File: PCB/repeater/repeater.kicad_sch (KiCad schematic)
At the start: 34 parts, among them J2 RF_IN, U1 DRA818V, U2 DRA818U, U3 PGA-103

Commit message: Continue routing
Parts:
- added C16: 6.8pF, symbol Device:C
- added C17: 12pF, symbol Device:C
- added C18: 10pF, symbol Device:C
- added C19, C20, C21, C22, C23: 100nF, symbol Device:C
- added C24: 10uF, symbol Device:C
- added J1: TX, symbol Connector:Conn_Coaxial
- added L7: 27nH, symbol Device:L
- added L8: 30nH, symbol Device:L
- added L9: 18nH, symbol Device:L
- added R4: 10k, symbol Device:R
- added R5: 10k, Resistor_SMD:R_0603_1608Metric_Pad0.98x0.95mm_HandSolder, symbol Device:R
- added RV1: 10k, symbol Device:R_Potentiometer
- added SW1: SW_Push, symbol Switch:SW_Push
- added U4: STM32F103C8Tx, Package_QFP:LQFP-48_7x7mm_P0.5mm, symbol MCU_ST_STM32F1:STM32F103C8Tx
- J2: value RF_IN -> RX
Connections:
- net AF_OUT: now also C15.1
- net GND: now also C16.2, C17.2, C18.2, C19.1, C20.1, C21.1, C22.1, C23.1, J1.2 (Ext), R5.2, RV1.3, SW1.1, U4.23 (VSS), U4.35 (VSS), U4.47 (VSS), U4.8 (VSSA)
- net VCC_3.3: now also C19.2, C20.2, C21.2, C22.2, C23.2, R4.1, U4.1 (VBAT), U4.24 (VDD), U4.36 (VDD), U4.48 (VDD), U4.9 (VDDA)
- net LPF_IN: now reaches U2.12 (ANT)
- net LPF_IN: now also C16.1, L7.1
- net at U2.18 (MIC_IN): now also RV1.1; no longer C15.2
- new net: C24.1, R4.2, SW1.2, U4.7 (NRST)
- new net: C15.2, RV1.2
- new net: R5.1, U4.44 (BOOT0)
- new net: C18.1, L8.2, L9.1
- new net: C17.1, L7.2, L8.1
- new net: J1.1 (In), L9.2
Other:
- note added: "Receiver BPF (~130MHz to ~150MHz)"
- note added: "Transmitter LPF"
- note added: "UHF Transmitter"
- note added: "Volume adjustment"
- note removed: "Receiver BPF"
- moved on the sheet: C15, D3, JP1, R2, R3, U2

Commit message: more work
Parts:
- added C25, C26: 15pF, symbol Device:C
- added C27, C28: 14pF, symbol Device:C
- added C29, C37, C38, C39, C40: 10uF, Capacitor_SMD:C_0603_1608Metric_Pad1.08x0.95mm_HandSolder, symbol Device:C
- added C30: 220nF, Capacitor_SMD:C_0603_1608Metric_Pad1.08x0.95mm_HandSolder, symbol Device:C
- added C31: 1uF, Capacitor_SMD:C_0603_1608Metric_Pad1.08x0.95mm_HandSolder, symbol Device:C
- added C32: 0.1uF, Capacitor_SMD:C_0603_1608Metric_Pad1.08x0.95mm_HandSolder, symbol Device:C
- added C33, C34, C35, C36: 22uF, Capacitor_SMD:C_0603_1608Metric_Pad1.08x0.95mm_HandSolder, symbol Device:C
- added C41, C42, C43, C44, C45, C46: 100nF, symbol Device:C
- added C47: 510nF, symbol Device:C
- added C48: 68nF, symbol Device:C
- added D4, D5, D6: LED, symbol Device:LED
- added FB1, FB2: FerriteBead, symbol Device:FerriteBead
- added J3: Conn_02x03_Counter_Clockwise, symbol Connector_Generic:Conn_02x03_Counter_Clockwise
- added L10: 8uH, lcsc:IND_BOURNS_SRP1250, symbol Device:L
- added L11: 33mH, symbol Device:L
- added L12: 240mH, symbol Device:L
- added R10: 24.9k, Resistor_SMD:R_0603_1608Metric_Pad0.98x0.95mm_HandSolder, symbol Device:R
- added R6, R7, R8: 1k, symbol Device:R
- added R9 (x2): 100k, Resistor_SMD:R_0603_1608Metric_Pad0.98x0.95mm_HandSolder, symbol Device:R
- added RV2: 10k, symbol Device:R_Potentiometer
- added SW2, SW3: SW_SPDT, symbol Switch:SW_SPDT
- added TP3 (x2): TestPoint, Connector_Pin:Pin_D1.1mm_L8.5mm_W2.5mm_FlatFork, symbol Connector:TestPoint
- added U5: LMR33630ADDA, Package_SO:Texas_HSOP-8-1EP_3.9x4.9mm_P1.27mm_ThermalVias, symbol Regulator_Switching:LMR33630ADDA
- added U6: AMS1117-3.3, Package_TO_SOT_SMD:SOT-223-3_TabPin2, symbol Regulator_Linear:AMS1117-3.3
- added U7: AMS1117-5.0, Package_TO_SOT_SMD:SOT-223-3_TabPin2, symbol Regulator_Linear:AMS1117-3.3
- added Y1: 32.768KHz 12.5pF, symbol Device:Crystal
- added Y2: 8MHz 12pF, symbol Device:Crystal_GND24
- C10, C9: value C -> 10pF
- C11: value 10pF -> 1000pF
- C2, C5: value C -> 3.3pF
- C3, C4: value C -> 9.1pF
- C6, C8: value C -> 2.7pF
- C7: value C -> 2.2pF
- L2, L3, L4, L5: value L -> 100nH
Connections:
- net BPF_IN: now also J2.1 (In)
- net BPF_OUT: now also C1.1, D1.3 (K), TP1.1
- net GND: now also C25.1, C26.1, C27.1, C28.1, C29.2, C30.2, C31.2, C33.2, C34.2, C35.2, C36.2, C37.2, C38.2, C39.2, C40.2, C41.1, C42.1, C43.1, C44.1, C45.1, C46.1, C48.1, D4.1 (K), D5.1 (K), D6.1 (K), J3.5 (Pin_5), L12.1, R10.2, RV2.3, U5.1 (GND), U5.9 (GND), U6.1 (GND), U7.1 (GND), Y2.2, Y2.4
- net PTT: now also U4.42 (PB6)
- net RXD_RX: now also U4.30 (PA9)
- net RXD_TX: now also U4.12 (PA2)
- net SQ: now also U4.43 (PB7)
- net TXD_RX: now also U4.31 (PA10)
- net TXD_TX: now also U4.13 (PA3)
- net VCC: now also C37.1, C40.1, C41.2, C42.2, C43.2, C44.2, C45.2, C46.2, FB1.2, SW3.1 (A), U6.3 (VI), U7.2 (VO)
- net VCC_3.3: now also FB2.2, J3.4 (Pin_4), R6.2, SW3.3 (C); no longer C12.2, C13.2, C14.2, L6.1
- net RST: now reaches C24.1, R4.2, SW1.2, U4.7 (NRST)
- net RST: now also J3.3 (Pin_3)
- net at RV1.1, U2.18 (MIC_IN): now also RV2.1
- net MORSE: now reaches U4.10 (PA0)
- net MORSE: now also RV2.2
- net RCC_OSC32_IN: now reaches U4.3 (PC14)
- net RCC_OSC32_IN: now also C26.2, Y1.1
- net SYS_JTMS-SWDIO: now reaches U4.34 (PA13)
- net SYS_JTMS-SWDIO: now also J3.1 (Pin_1)
- net SYS_JTCK-SWCLK: now reaches U4.37 (PA14)
- net SYS_JTCK-SWCLK: now also J3.2 (Pin_2)
- net RCC_OSC32_OUT: now reaches U4.4 (PC15)
- net RCC_OSC32_OUT: now also C25.2, Y1.2
- net LED_TX: now reaches U4.45 (PB8)
- net LED_TX: now also R7.2
- net LED_RX: now reaches U4.46 (PB9)
- net LED_RX: now also R8.2
- net X_IN: now reaches U4.5 (PD0)
- net X_IN: now also C28.2, Y2.3
- net X_OUT: now reaches U4.6 (PD1)
- net X_OUT: now also C27.2, Y2.1
- new net: D5.2 (A), R7.1
- new net: C12.2, C13.2, C14.2, L6.1, SW3.2 (B)
- new net: C33.1, C34.1, C35.1, C36.1, FB1.1, L10.2, R9.1, TP3.1
- new net: R10.1, R9.2, U5.5 (FB)
- new net: C38.1, FB2.1, U6.2 (VO)
- new net: D4.2 (A), R6.1
- new net: C29.1, C30.1, SW2.1 (A), U5.2 (VIN), U5.3 (EN)
- new net: C31.1, R9.2, U5.6 (VCC)
- new net: C32.1, U5.7 (BOOT)
- new net: C32.2, L10.1, U5.8 (SW)
- new net: C39.1, SW2.3 (C), U7.3 (VI)
- new net: D6.2 (A), R8.1
- new net: C47.2, L11.1
- new net AUDIO_FILTER_IN: C47.1
- new net AUDIO_FILTER_OUT: C48.2, L11.2, L12.2
- new net PG: R9.1, TP3.1, U5.4 (PG)
- new net VCC_IN: J3.6 (Pin_6), SW2.2 (B)
- no-connect marks 4 -> 26
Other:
- note added: "Audio Conditioning Filter (~300Hz to 5KHz)"
- note added: "MCU"
- note added: "No, this is not a mistake - it's either floating or LOW for some reason"
- note added: "Oh boy do I love the 'ol AVR ISP headers"
- note added: "Power supply"
- note added: "Protection diodes...."
- note added: "Theoretical response @200 ohm input 680 ohms output, which is my best guess at the audio impedance"
- note added: "This switch decides how much power we feed into the LNA. More voltage = better gain but also more noise."
- note added: "This switch decides how we generate the 5V rail - SMPS or LDO?"
- note added: "Transmitter LPF ~(465MHz)"
- note added: "Volume adjustment of morse identification"
- note added: "Volume adjustment of repeater"
- note removed: "Transmitter LPF"
- note removed: "Volume adjustment"
- moved on the sheet: C10, C19, C2, C20, C21, C22, C23, C24, C3, C4, C5, C6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

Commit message: Add filter and switch
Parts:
- added SW4: SW_SPDT, symbol Switch:SW_SPDT
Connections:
- net AUDIO_FILTER_IN: now also C15.2, SW4.3 (C)
- net AUDIO_FILTER_OUT: now also SW4.1 (A)
- net at RV1.2: now also SW4.2 (B); no longer C15.2
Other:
- note added: "Switch to turn audio filter on/off"
- moved on the sheet: C15, C44, C45, C46, D2, R1, U1

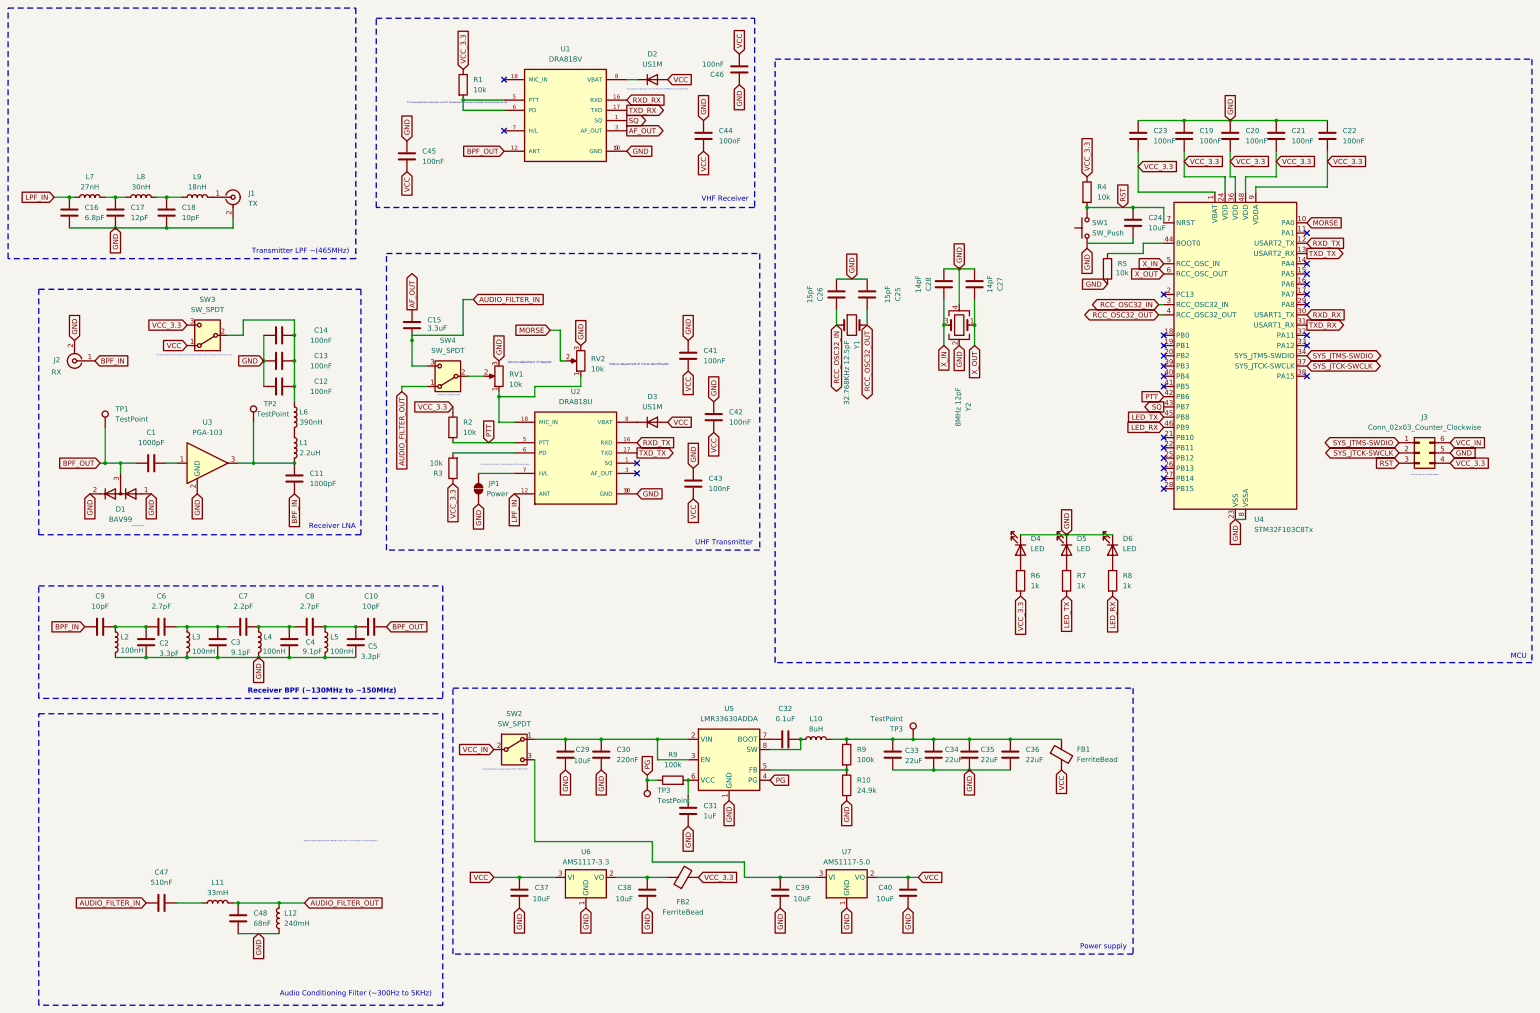
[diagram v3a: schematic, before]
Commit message: Add PD reset pins for all DRA818s
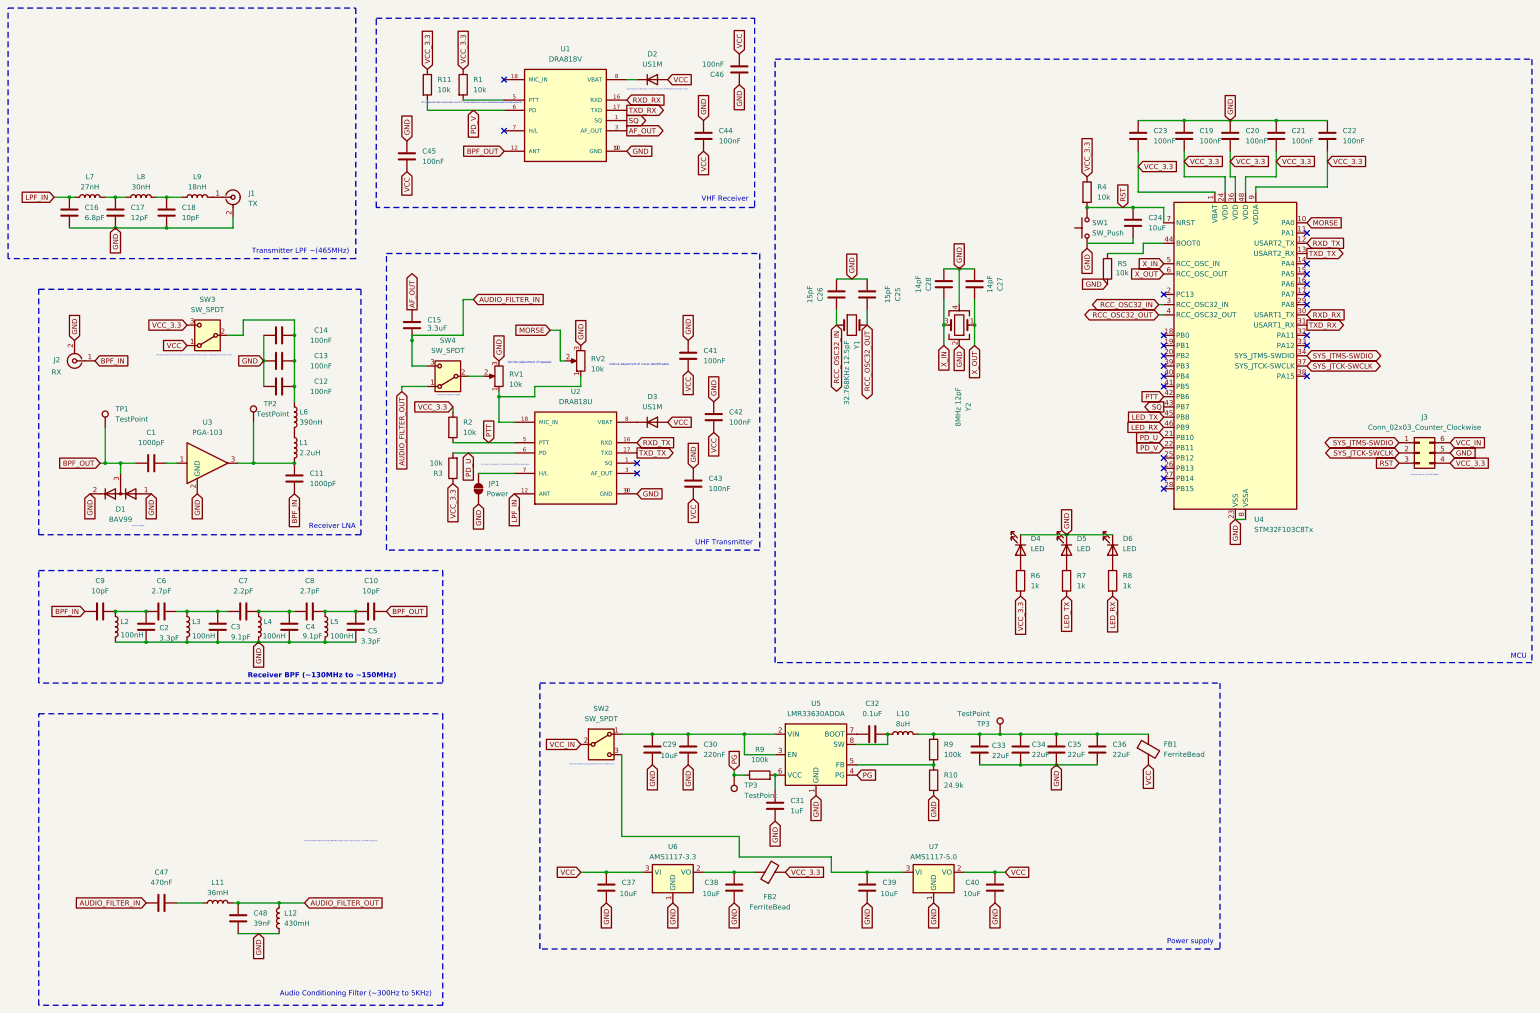
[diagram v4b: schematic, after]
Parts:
- added R11: 10k, symbol Device:R
- C47: value 510nF -> 470nF
- C48: value 68nF -> 39nF
- L11: value 33mH -> 36mH
- L12: value 240mH -> 430mH
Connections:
- net VCC_3.3: now also R11.1
- net PD_U: now reaches R3.2, U2.6 (PD)
- net PD_U: now also U4.21 (PB10)
- net at R1.2, U1.5 (PTT): no longer U1.6 (PD)
- net PD_V: now reaches U4.22 (PB11)
- net PD_V: now also U1.6 (PD), R11.2
- no-connect marks 26 -> 24
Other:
- moved on the sheet: C10, C2, C29, C3, C30, C31, C32, C33, C34, C35, C36, C37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

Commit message: Oops... reannotate schematic
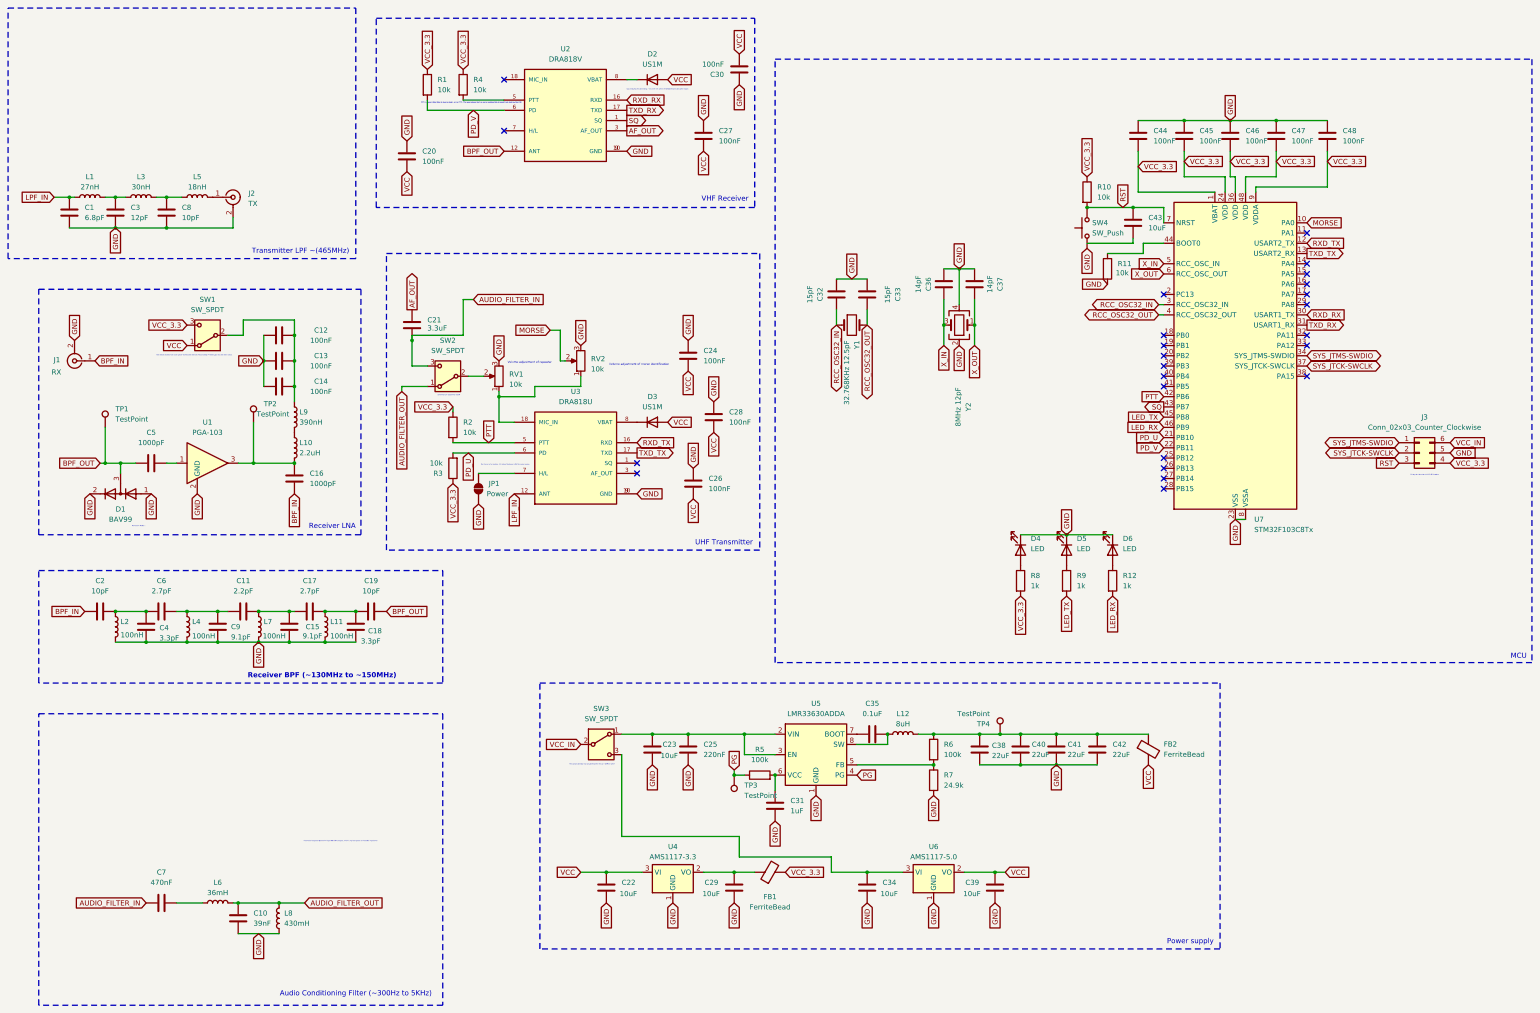
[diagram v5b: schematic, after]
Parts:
- renumbered C16 to C1, C48 to C10, C7 to C11, C14 to C12, C12 to C14, C4 to C15, C11 to C16, C8 to C17, C5 to C18, C10 to C19, C9 to C2, C45 to C20, C15 to C21, C37 to C22, C29 to C23, C41 to C24, C30 to C25, C43 to C26, C44 to C27, C42 to C28, C38 to C29, C17 to C3, C46 to C30, C26 to C32, C25 to C33, C39 to C34, C32 to C35, C28 to C36, C27 to C37, C33 to C38, C40 to C39, C2 to C4, C34 to C40, C35 to C41, C36 to C42, C24 to C43, C23 to C44, C19 to C45, C20 to C46, C21 to C47, C22 to C48, C1 to C5, C47 to C7, C18 to C8, C3 to C9, FB2 to FB1, FB1 to FB2, J2 to J1, J1 to J2, L7 to L1, L1 to L10, L5 to L11, L10 to L12, L8 to L3, L3 to L4, L9 to L5, L11 to L6, L4 to L7, L12 to L8, L6 to L9, R11 to R1, R4 to R10, R5 to R11, R8 to R12, R1 to R4, R9 to R5, R9 to R6, R10 to R7, R6 to R8, R7 to R9, SW3 to SW1, SW4 to SW2, SW2 to SW3, SW1 to SW4, TP3 to TP4, U3 to U1, U1 to U2, U2 to U3, U6 to U4, U7 to U6, U4 to U7
